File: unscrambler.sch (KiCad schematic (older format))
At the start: 10 parts, among them U11 74HC14, U12 74HC164, U5 74HC74, U6 74HC86, U7 74HC164

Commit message: Final parts placement and verified net against an actual Issue 3 board.
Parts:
- C12: Type 20% Monolithic -> 20% Monolithic Ceramic
- C23: footprint Capacitors_THT:C_Axial_L3.8mm_D2.6mm_P10.00mm_Horizontal -> Capacitors_THT:C_Disc_D3.0mm_W2.0mm_P2.50mm; Type 2.5% polystyrene -> 20% monolithic ceramic
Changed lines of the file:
@@
 F 0 "C23" H 8965 3696 50  0000 L CNN
 F 1 ".001uF" H 8965 3605 50  0000 L CNN
-F 2 "Capacitors_THT:C_Axial_L3.8mm_D2.6mm_P10.00mm_Horizontal" H 8888 3500 50  0001 C CNN
+F 2 "Capacitors_THT:C_Disc_D3.0mm_W2.0mm_P2.50mm" H 8888 3500 50  0001 C CNN
 F 3 "" H 8850 3650 50  0001 C CNN
-F 4 "2.5% polystyrene" V 8850 3650 60  0001 C CNN "Type"
+F 4 "20% monolithic ceramic" V 8850 3650 60  0001 C CNN "Type"
 	1    8850 3650
 	1    0    0    -1
@@
 F 2 "Capacitors_THT:C_Disc_D3.0mm_W2.0mm_P2.50mm" H 4038 5000 50  0001 C CNN
 F 3 "" H 4000 5150 50  0001 C CNN
-F 4 "20% Monolithic" H 4000 5150 60  0001 C CNN "Type"
+F 4 "20% Monolithic Ceramic" H 4000 5150 60  0001 C CNN "Type"
 	1    4000 5150
 	0    1    1    0

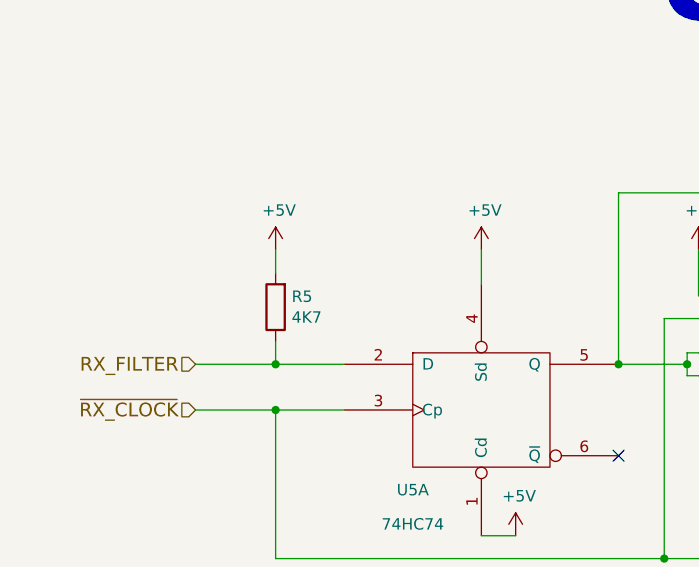
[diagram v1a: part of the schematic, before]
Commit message: Corrected transcription errors.
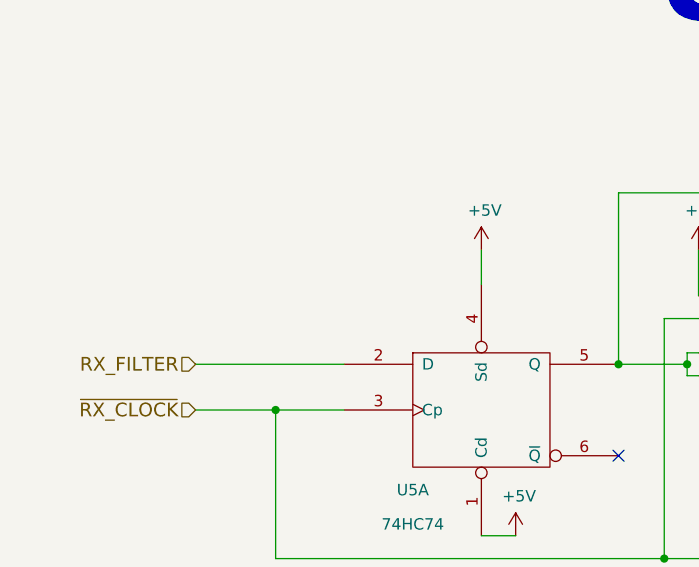
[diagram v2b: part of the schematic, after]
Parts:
- removed R5: 4K7, Resistors_THT:R_Axial_DIN0204_L3.6mm_D1.6mm_P7.62mm_Horizontal, symbol R
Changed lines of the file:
@@
 $EndDescr
-$Comp
-L R R5
-U 1 1 5984DB20
-P 1550 3800
-F 0 "R5" H 1480 3754 50  0000 R CNN
-F 1 "4K7" H 1480 3845 50  0000 R CNN
-F 2 "Resistors_THT:R_Axial_DIN0204_L3.6mm_D1.6mm_P7.62mm_Horizontal" V 1480 3800 50  0001 C CNN
-F 3 "" H 1550 3800 50  0001 C CNN
-	1    1550 3800
-	-1   0    0    1
-$EndComp
 $Comp
 L 74HC74 U5
@@
 F 3 "" H 2600 4800 50  0001 C CNN
 	1    2600 4800
-	1    0    0    -1
-$EndComp
-$Comp
-L +5V #PWR040
-U 1 1 5984DB41
-P 1550 3550
-F 0 "#PWR040" H 1550 3400 50  0001 C CNN
-F 1 "+5V" H 1565 3723 50  0000 C CNN
-F 2 "" H 1550 3550 50  0001 C CNN
-F 3 "" H 1550 3550 50  0001 C CNN
-	1    1550 3550
 	1    0    0    -1
 $EndComp
@@
 NoConn ~ 6100 4050
 NoConn ~ 7600 4550
-Connection ~ 1550 4050
 Wire Wire Line
 	1200 4050 1850 4050
@@
 Wire Wire Line
 	2450 3550 2450 3700
-Wire Wire Line
-	1550 3550 1550 3650
 Wire Wire Line
 	3400 4000 3350 4000
@@
 Wire Wire Line
 	8850 3800 8850 3850
-Wire Wire Line
-	1550 4050 1550 3950
 Text HLabel 1200 4050 0    60   Input ~ 0
 RX_FILTER
